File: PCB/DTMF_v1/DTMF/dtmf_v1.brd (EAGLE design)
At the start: 60 x 30 mm, 28 parts, among them IC1 ATTINY84A-SSF, IC2 MT8870DS1, Y1 ATS080B-E, Y2 ATS080B-E

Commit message: vault backup: 2023-12-27 10:32:53
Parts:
- removed L1, L2, L3, L4: (no value), adafruit:CHIP-LED0805
- removed R4, R5, R6, R7: 330, rcl:M0805
- added L5: (no value), adafruit:CHIP-LED0805
- added R11: 330, rcl:M0805
- added TP1, TP2, TP4, TP5, TP7: PTR1B1,27, testpad:B1,27
- added USER_IN_2: (no value), pinhead:1X02
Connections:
- removed net N$17: L4.C, R7.1
- removed net N$20: L1.C, R4.1
- removed net N$6: IC1.12, IC2.13, L2.A
- removed net N$8: IC1.10, IC2.11, L4.A
- new net CUTDOWN: USER_IN_2.1
- new net N$25: L5.C, R11.1
- net GND: now also R11.2; no longer R4.2, R5.2, R6.2, R7.2
- net N$18: now also IC1.10, IC2.11, TP5.TP; no longer L3.C, R6.1
- net N$19: now also IC1.12, IC2.13, TP2.TP; no longer L2.C, R5.1
- net N$24: now also USER_IN_2.2
- net N$4: now also L5.A, TP7.TP
- net N$5: now also TP1.TP; no longer L1.A
- net N$7: now also TP4.TP; no longer L3.A
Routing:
- net VCC: track 73.9 -> 0.00 mm
- net SCL: track 62.9 -> 0.00 mm, vias 1 -> 0
- net N$8: track 51.4 -> 0.00 mm
- net SDA: track 50.1 -> 0.00 mm, vias 1 -> 0
- net N$11: track 40.3 -> 0.00 mm
- net N$7: track 35.0 -> 0.00 mm, vias 2 -> 0
- net N$6: track 34.2 -> 0.00 mm, vias 2 -> 0
- net RESET: track 33.1 -> 0.00 mm
- net N$5: track 32.2 -> 0.00 mm, vias 2 -> 0
- net N$4: track 26.8 -> 0.00 mm, vias 2 -> 0
- net N$10: track 23.0 -> 0.00 mm, vias 1 -> 0
- net N$24: track 21.6 -> 0.00 mm, vias 1 -> 0
- net N$9: track 18.8 -> 0.00 mm
- net AUDIO: track 16.1 -> 0.00 mm
- net N$22: track 15.6 -> 0.00 mm
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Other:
- board size 60 x 30 mm -> 100 x 30 mm

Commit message: modifications done on mac for the board
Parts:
- removed USER_IN_2: (no value), pinhead:1X02
- added JP2: (no value), pinhead:2X02
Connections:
- new net DROGUE: JP2.4
- net CUTDOWN: now also JP2.2; no longer USER_IN_2.1
- net N$22: now also JP2.3
- net N$24: now also JP2.1; no longer USER_IN_2.2
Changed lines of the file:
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@@
 <attribute name="VALUE" x="11.43" y="22.452" size="1.27" layer="28" rot="MR270" align="center"/>
-</element>
-<element name="USER_IN_2" library="pinhead" library_urn="urn:adsk.eagle:library:325" package="1X02" package3d_urn="urn:adsk.eagle:package:22435/2" value="" x="58.166" y="10.16" smashed="yes">
-<attribute name="NAME" x="55.5498" y="11.9888" size="1.27" layer="25" ratio="10"/>
-<attribute name="POPULARITY" value="98" x="58.166" y="10.16" size="1.778" layer="27" display="off"/>
-<attribute name="VALUE" x="55.626" y="6.985" size="1.27" layer="27"/>
 </element>
 <element name="L5" library="adafruit" package="CHIP-LED0805" value="" x="25.908" y="8.636" smashed="yes" rot="R180">
@@
 <attribute name="TP_SIGNAL_NAME" value="" x="23.622" y="6.604" size="1.778" layer="27" display="off"/>
 <attribute name="VALUE" x="22.352" y="5.207" size="0.0254" layer="27"/>
+</element>
+<element name="JP2" library="pinhead" library_urn="urn:adsk.eagle:library:325" package="2X02" package3d_urn="urn:adsk.eagle:package:22455/2" value="" x="-13.208" y="-1.016" smashed="yes">
+<attribute name="NAME" x="-15.748" y="2.159" size="1.27" layer="25" ratio="10"/>
+<attribute name="POPULARITY" value="0" x="-13.208" y="-1.016" size="1.778" layer="27" display="off"/>
+<attribute name="VALUE" x="-15.748" y="-5.461" size="1.27" layer="27"/>
 </element>
 </elements>
@@
 </signal>
 <signal name="N$22">
-<contactref element="IC1" pad="6"/>
 <contactref element="USER_INT" pad="1"/>
 <contactref element="LED5" pad="A"/>
+<contactref element="IC1" pad="6"/>
+<contactref element="JP2" pad="3"/>
 <wire x1="47.13" y1="18.009" x2="47.532" y2="21.59" width="0" layer="19" extent="1-1"/>
 <wire x1="42.418" y1="23.622" x2="47.532" y2="21.59" width="0" layer="19" extent="1-1"/>
+<wire x1="-11.938" y1="-2.286" x2="42.418" y2="23.622" width="0" layer="19" extent="1-1"/>
 </signal>
 <signal name="N$23">
@@
 <contactref element="IC1" pad="8"/>
 <contactref element="ICSP1" pad="1"/>
-<contactref element="USER_IN_2" pad="2"/>
-<wire x1="59.436" y1="10.16" x2="55.45" y2="26.818" width="0" layer="19" extent="1-1"/>
-<wire x1="45.86" y1="12.587" x2="59.436" y2="10.16" width="0" layer="19" extent="1-1"/>
-</signal>
-<signal name="CUTDOWN">
-<contactref element="USER_IN_2" pad="1"/>
+<contactref element="JP2" pad="1"/>
+<wire x1="45.86" y1="12.587" x2="55.45" y2="26.818" width="0" layer="19" extent="1-1"/>
+<wire x1="-14.478" y1="-2.286" x2="45.86" y2="12.587" width="0" layer="19" extent="1-1"/>
 </signal>
 <signal name="N$25">
@@
 <wire x1="21.844" y1="8.382" x2="22.818" y2="14.28" width="0" layer="19" extent="1-1"/>
 </signal>
+<signal name="CUTDOWN">
+<contactref element="JP2" pad="2"/>
+</signal>
+<signal name="DROGUE">
+<contactref element="JP2" pad="4"/>
+</signal>
 </signals>

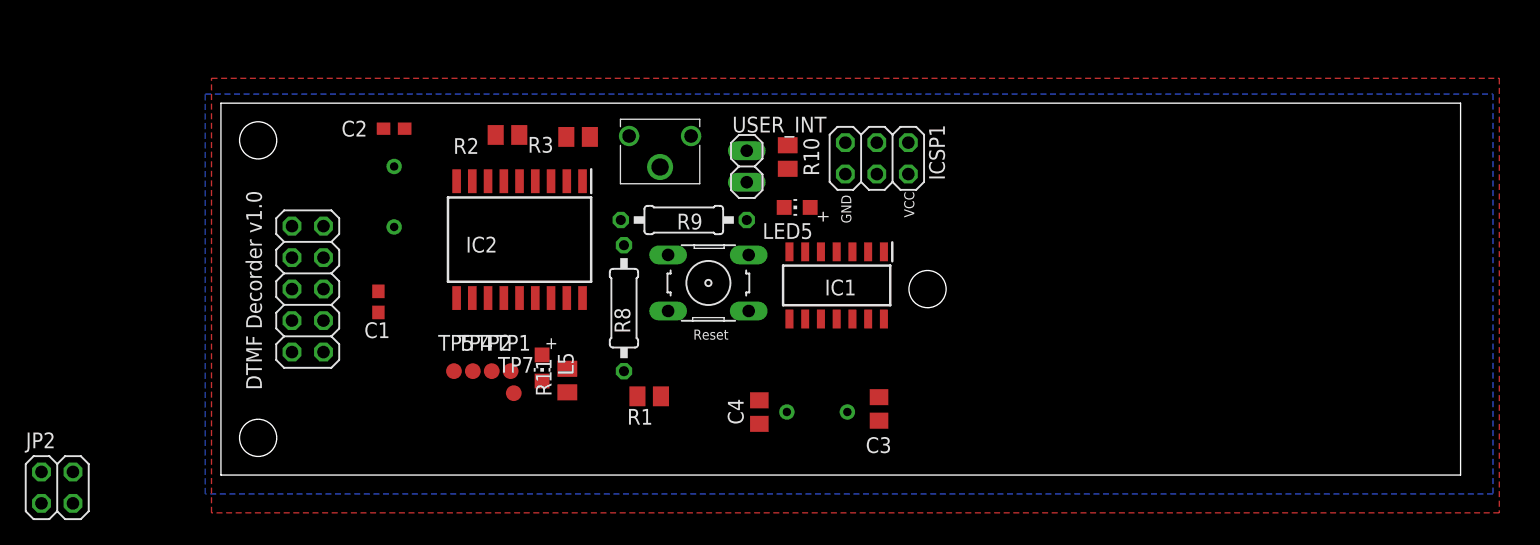
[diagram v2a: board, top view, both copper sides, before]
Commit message: DTMF v1 completed with cutdown 30x100 mm form factor
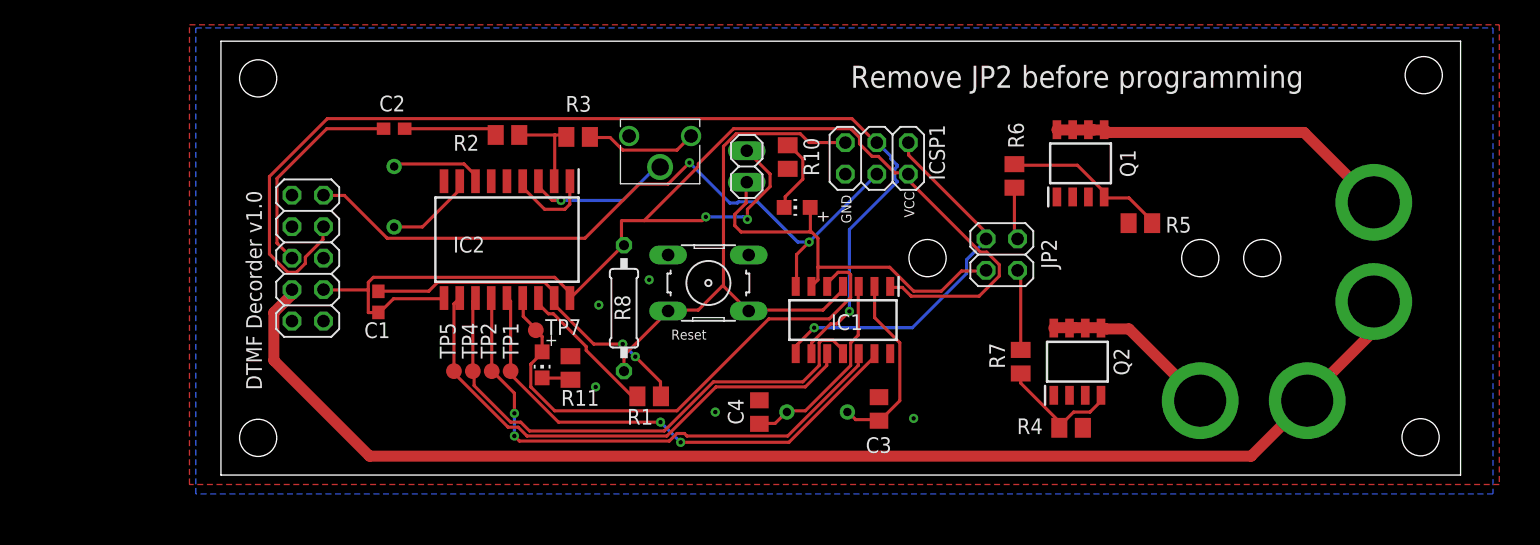
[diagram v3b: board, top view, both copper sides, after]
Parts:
- removed R9: 10k, rcl:0207/10
- added Q1, Q2: MCQ4438-TP, MCQ4438-TP:SOIC127P600X175-8N
- added R4: 100k, rcl:M0805
- added R5: 100 k, rcl:M0805
- added R6, R7: 1 k, rcl:M0805
- added U$1, U$2, U$3, U$4: M3_HOLE, KE8TJE:MOUNTING_PAD
- R2: value (none) -> 100 k
- R3: value (none) -> 300 k
- moved JP2 78.5 mm to (63.0, 17.8), turned to 270 degrees
- moved TP7 5.38 mm to (25.4, 11.7)
- moved IC1 2.84 mm to (50.2, 12.5)
- moved JP1 2.50 mm to (7.00, 17.5)
- moved R11 1.05 mm to (28.2, 8.64)
- moved IC2 1.02 mm to (23.1, 19.0)
- moved L5 0.25 mm to (25.9, 8.89)
- renumbered USER_INT to JP3
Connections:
- removed net N$21: JP3.2, R9.1
- new net N$17: Q2.5, Q2.6, Q2.7, Q2.8, U$4.P$1
- new net N$20: Q1.5, Q1.6, Q1.7, Q1.8, U$2.P$1
- new net N$27: Q2.4, R4.2, R7.2
- new net N$6: Q1.4, R5.2, R6.1
- net CUTDOWN: now also R6.2
- net DROGUE: now also R7.1
- net GND: now also Q1.1, Q1.2, Q1.3, Q2.1, Q2.2, Q2.3, R4.1, R5.1
- net VCC: now also JP3.2; no longer R9.2
- net V_BAT: now also U$1.P$1, U$3.P$1
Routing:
- net V_BAT: track 0.00 -> 104.9 mm
- net VCC: track 0.00 -> 103.5 mm, vias 0 -> 2
- net SCL: track 0.00 -> 86.4 mm, vias 0 -> 1
- net SDA: track 0.00 -> 57.7 mm, vias 0 -> 2
- net RESET: track 0.00 -> 44.9 mm
- net N$19: track 0.00 -> 43.5 mm, vias 0 -> 2
- net N$7: track 0.00 -> 43.2 mm
- net N$4: track 0.00 -> 43.0 mm
- net N$18: track 0.00 -> 41.9 mm
- net N$5: track 0.00 -> 41.1 mm, vias 0 -> 2
- net N$22: track 0.00 -> 32.2 mm
- net N$24: track 0.00 -> 30.7 mm, vias 0 -> 1
- net N$11: track 0.00 -> 28.2 mm, vias 0 -> 2
- net N$20: track 0.00 -> 28.0 mm
- net AUDIO: track 0.00 -> 17.2 mm
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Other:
- board size 100 x 30 mm -> 100 x 35 mm
- board text added: "DTMF decorder - v1.0 KE8TJE - Jan 24"
- board text added: "Remove JP2 before programming"
- board text removed: "DTMF decorder - v1.0 KE8TJE - Jan 23"

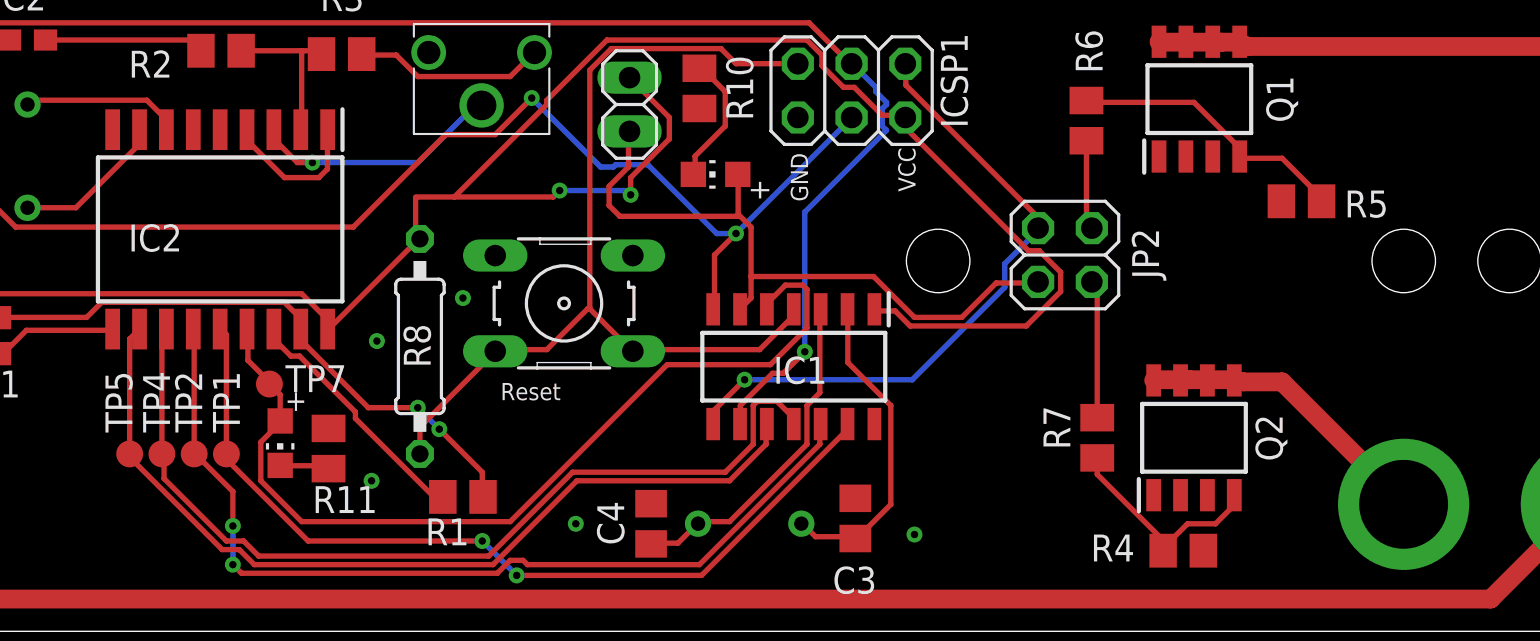
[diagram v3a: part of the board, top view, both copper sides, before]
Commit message: cleaned the schematic for documentation
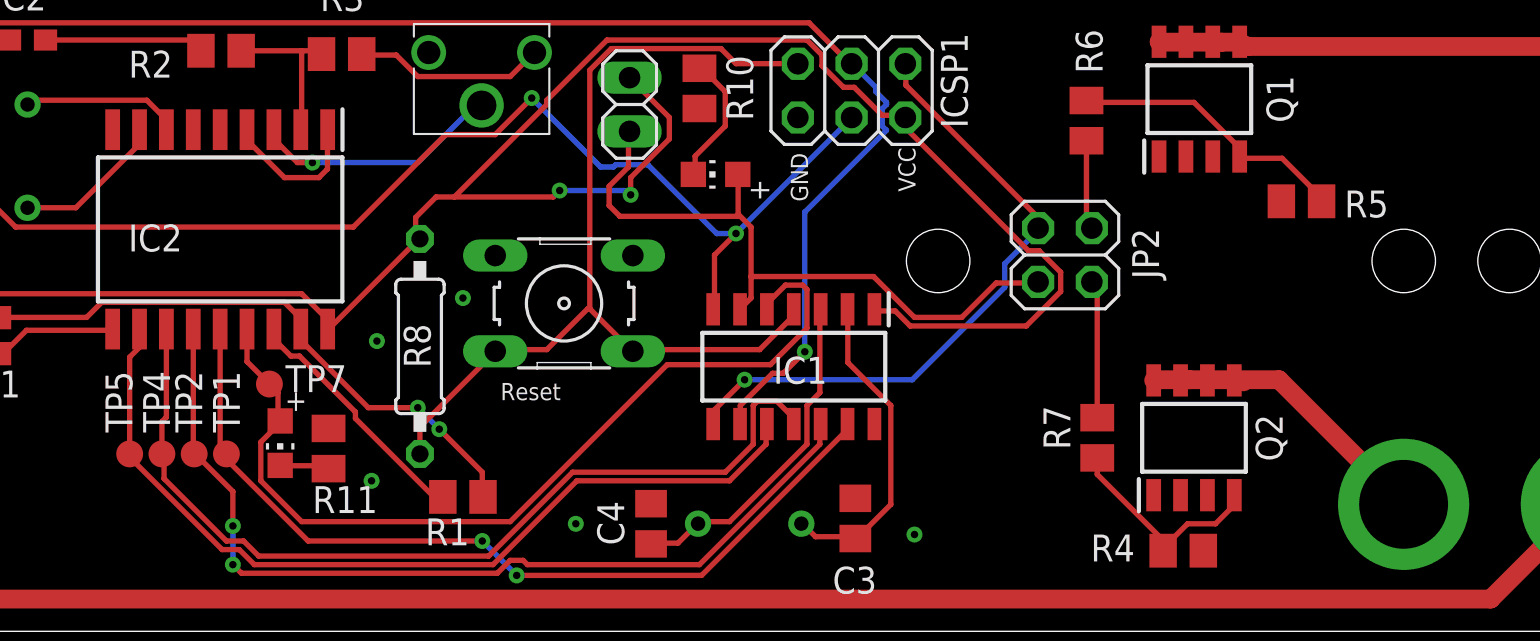
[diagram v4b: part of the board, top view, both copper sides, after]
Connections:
- net N$18 renamed Q1
- net N$19 renamed Q3
- net N$4 renamed TONE_PRESENT
- net N$5 renamed Q4
- net N$7 renamed Q2
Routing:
- net Q4: track 41.1 -> 41.6 mm
- net N$17: track 14.3 -> 14.8 mm

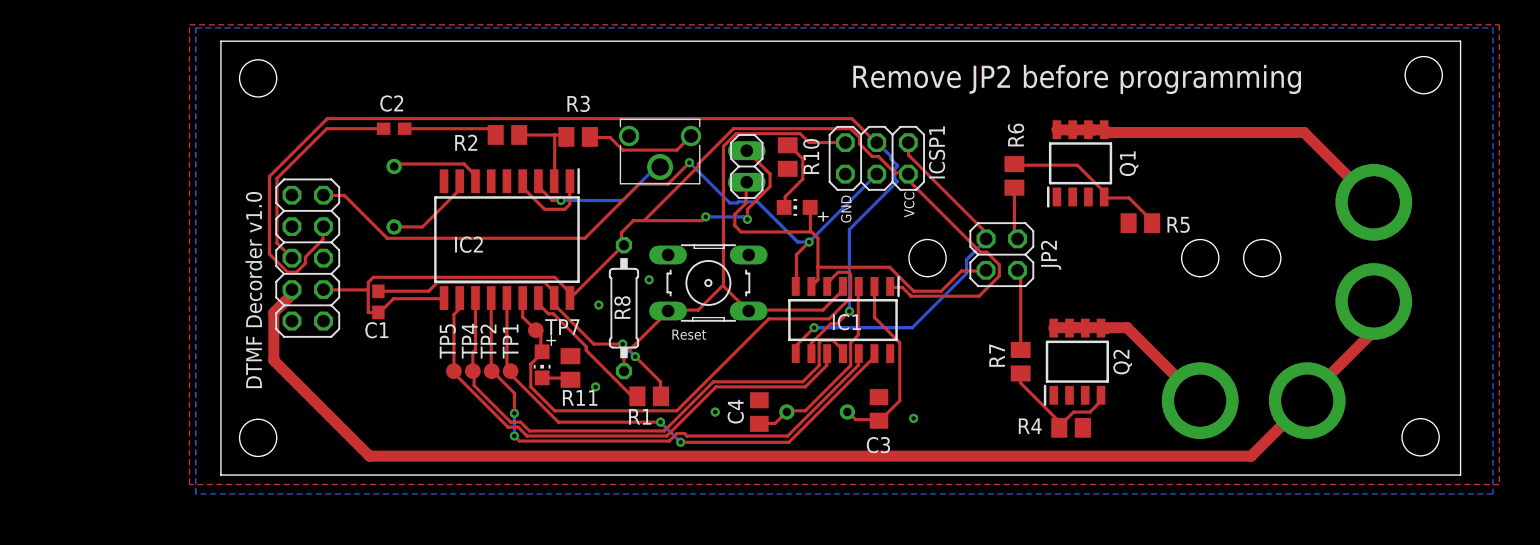
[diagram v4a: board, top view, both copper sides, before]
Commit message: modified PCB with JLC DRC file
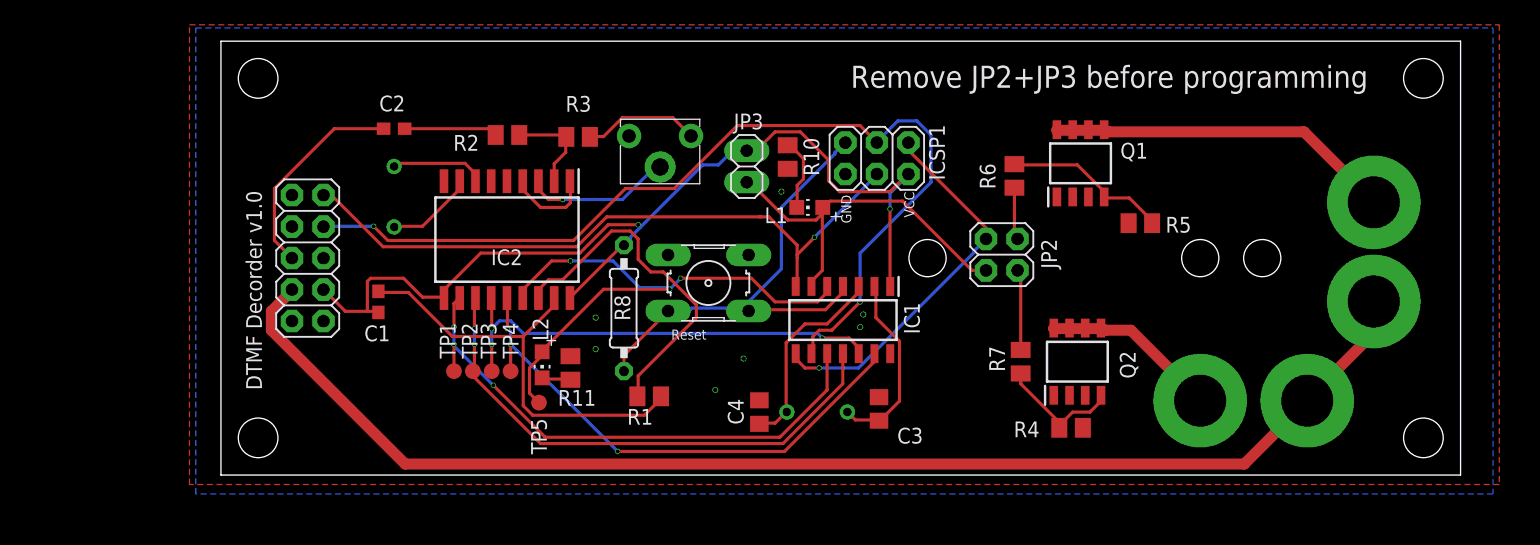
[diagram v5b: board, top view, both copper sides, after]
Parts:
- removed LED5: (no value), adafruit:CHIP-LED0805
- removed TP7: PTR1B1,27, testpad:B1,27
- added L1: (no value), adafruit:CHIP-LED0805
- added TP3: PTR1B1,27, testpad:B1,27
- Q1, Q2: value MCQ4438-TP -> MCQ4406A-TP; device MCQ4438-TP:SOIC127P600X175-8N -> MCQ4406A-TP:SOIC127P600X175-8N
- R5: value 100 k -> 100k
- R6, R7: value 1 k -> 1k
- moved TP5 7.31 mm to (25.7, 5.84)
- moved TP1 4.57 mm to (18.8, 8.38)
- moved TP4 3.05 mm to (23.4, 8.38)
- moved TP2 1.52 mm to (20.3, 8.38)
- renumbered L5 to L2
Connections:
- net N$22: now also L1.A; no longer LED5.A
- net N$23: now also L1.C; no longer LED5.C
- net Q1: now also TP1.TP; no longer TP5.TP
- net Q2: now also TP2.TP; no longer TP4.TP
- net Q3: now also TP3.TP; no longer TP2.TP
- net Q4: now also TP4.TP; no longer TP1.TP
- net TONE_PRESENT: now also TP5.TP; no longer TP7.TP
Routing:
- net VCC: track 103.1 -> 79.6 mm
- net N$12: track 11.7 -> 28.2 mm
- net SCL: track 86.4 -> 77.4 mm, vias 1 -> 2
- net N$11: track 28.2 -> 35.2 mm, vias 2 -> 0
- net Q3: track 43.6 -> 37.2 mm, vias 2 -> 3
- net RESET: track 44.9 -> 38.6 mm
- net TONE_PRESENT: track 43.3 -> 46.4 mm, vias 0 -> 3
- net SDA: track 57.7 -> 54.5 mm, vias 2 -> 1
- net N$22: track 32.2 -> 30.1 mm
- net Q1: track 41.9 -> 43.9 mm, vias 0 -> 3
- net Q4: track 41.6 -> 42.6 mm, vias 2 -> 3
- net V_BAT: track 104.9 -> 104.3 mm
- net Q2: track 43.2 -> 42.9 mm, vias 0 -> 2
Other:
- board text added: "Remove JP2+JP3 before programming"
- board text removed: "Remove JP2 before programming"

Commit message: added openhw log,slot for internal leds
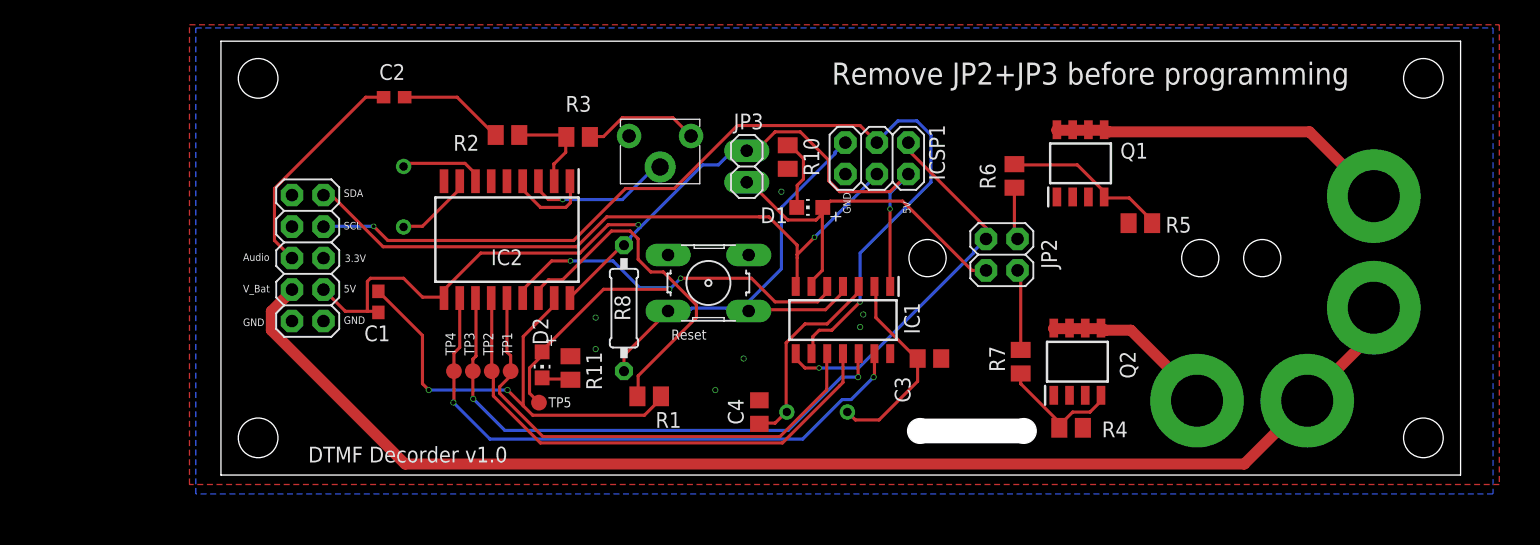
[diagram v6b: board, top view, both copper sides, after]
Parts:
- moved C3 5.75 mm to (57.1, 9.40), turned to 0 degrees
- moved TP1 4.57 mm to (23.4, 8.38)
- moved TP4 4.57 mm to (18.8, 8.38)
- moved C2 2.54 mm to (14.0, 30.5)
- moved TP2 1.52 mm to (21.8, 8.38)
- moved TP3 1.52 mm to (20.3, 8.38)
- moved Y2 0.76 mm to (14.7, 24.9)
- moved U$1 0.50 mm to (93.0, 13.5)
- moved U$2 0.50 mm to (93.0, 22.5)
- moved U$4 0.25 mm to (78.7, 6.00)
- renumbered L1 to D1, L2 to D2
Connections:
- net Q1: now also IC2.14; no longer IC2.11
- net Q2: now also IC2.13; no longer IC2.12
- net Q3: now also IC2.12; no longer IC2.13
- net Q4: now also IC2.11; no longer IC2.14
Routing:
- net Q3: track 37.2 -> 44.1 mm, vias 3 -> 2
- net Q4: track 42.6 -> 47.8 mm, vias 3 -> 2
- net N$11: track 35.2 -> 39.7 mm, vias 0 -> 2
- net Q1: track 43.9 -> 40.5 mm, vias 3 -> 0
- net N$15: track 7.55 -> 8.61 mm
- net AUDIO: track 17.0 -> 18.0 mm
- net N$9: track 15.4 -> 16.4 mm
- net Q2: track 42.9 -> 42.1 mm, vias 2 -> 0
- net N$2: track 7.22 -> 6.46 mm
- net N$1: track 7.63 -> 6.87 mm
- net V_BAT: track 104.3 -> 103.8 mm
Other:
- outline, holes or cut-outs redrawn
- board text added: "/home/hasith/Pictures/NEBP/open_hw2.bmp"
- board text added: "/home/hasith/Pictures/NEBP/open_hw3.bmp"
- board text added: "3.3V"
- board text added: "5V"
- board text added: "Audio"
- board text added: "SCL"
- board text added: "SDA"
- board text added: "V_Bat"
- board text removed: "VCC"

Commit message: final board design
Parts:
- renumbered ICSP1 to ICSP
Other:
- outline, holes or cut-outs redrawn
